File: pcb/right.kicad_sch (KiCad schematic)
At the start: 73 parts, among them J2 AudioJack3, SW22 Y, SW23 U, SW24 I, SW25 O, SW26 P, SW27 BS, SW28 H, SW29 J, SW30 K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

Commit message: Rewire left half
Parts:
- SW49: value T -> EX3
- SW50: value G -> EX4
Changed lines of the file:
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@@
 			)
 		)
-		(property "Value" "T"
+		(property "Value" "EX3"
 			(at 171.45 58.42 0)
 			(effects
@@
 			)
 		)
-		(property "Value" "G"
+		(property "Value" "EX4"
 			(at 171.45 83.82 0)
 			(effects

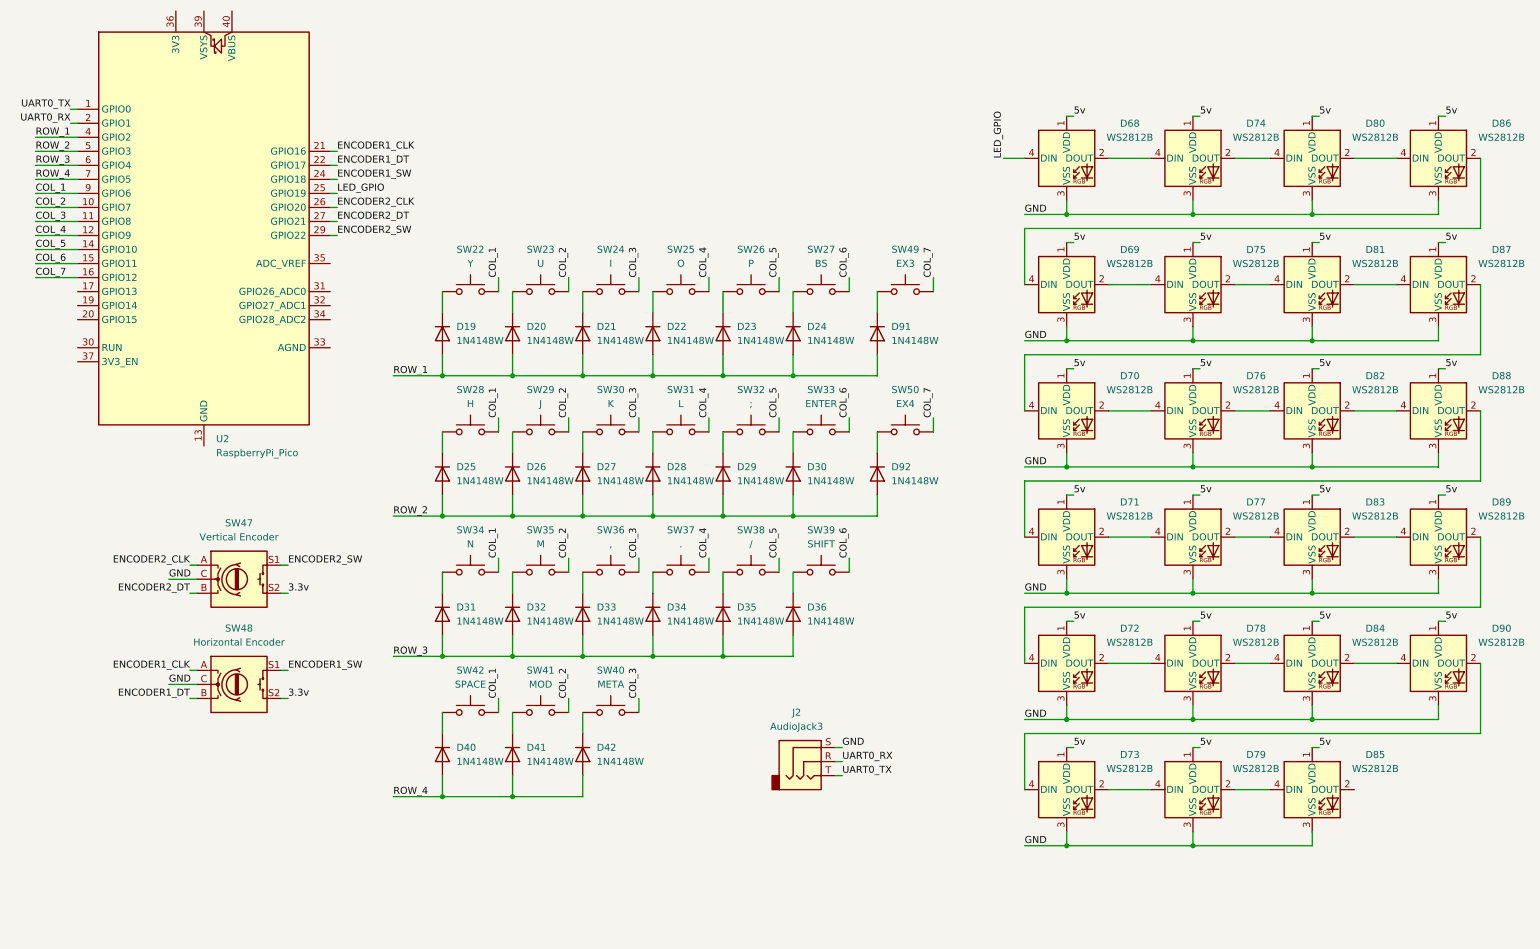
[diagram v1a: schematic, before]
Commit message: Move row and column to start with 0 on schematic
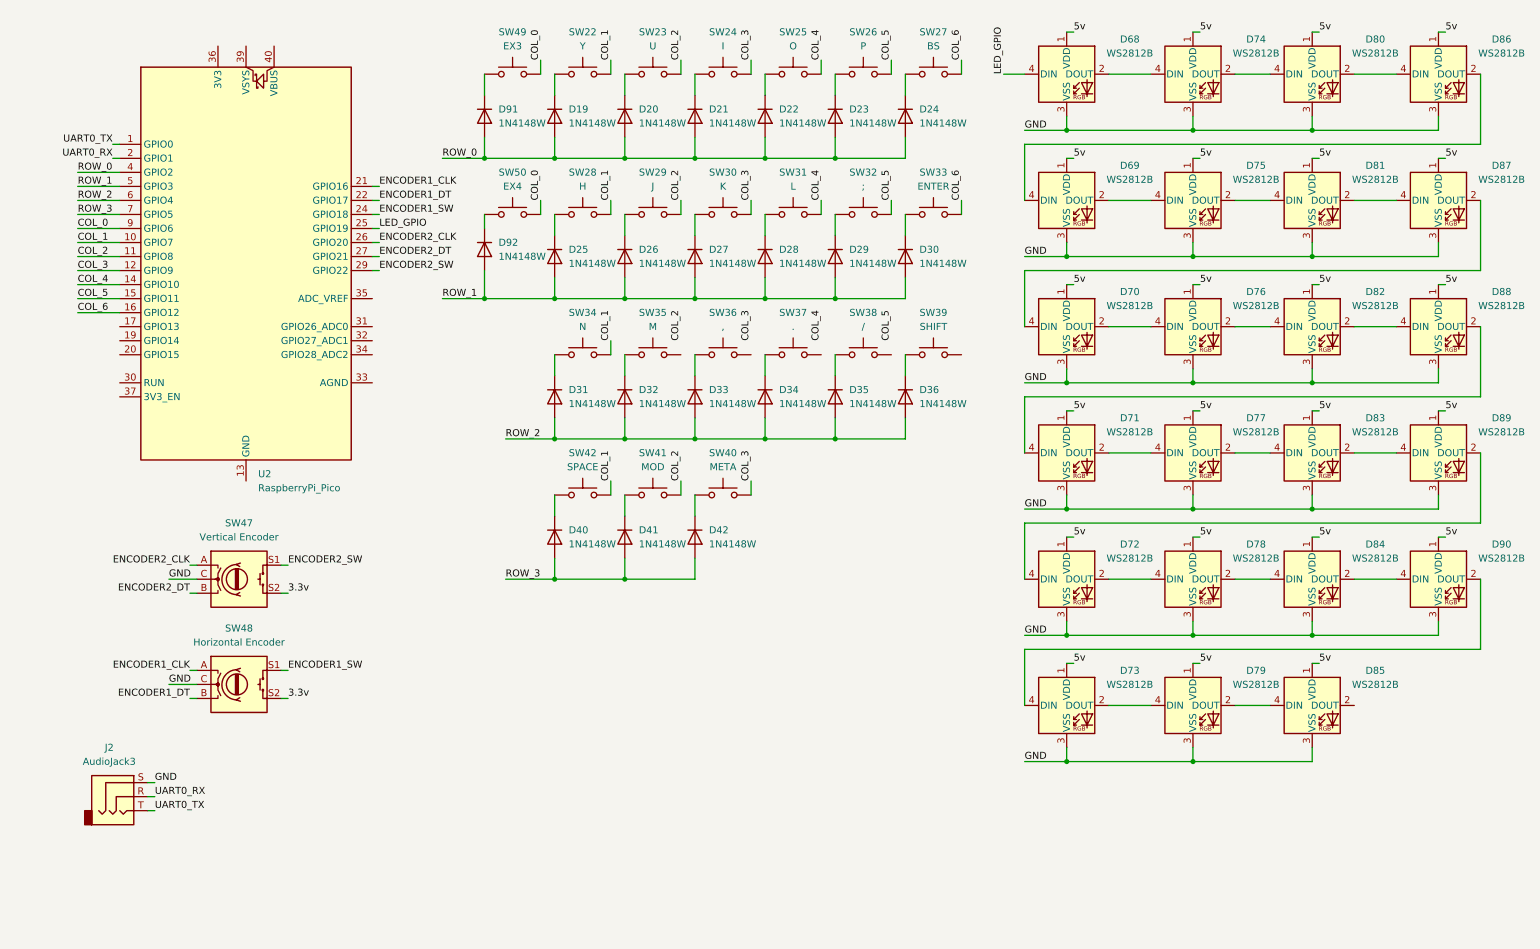
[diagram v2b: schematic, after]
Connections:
- net ROW_4 is gone; now on net ROW_3: D40.2 (A), D41.2 (A), D42.2 (A), U2.7 (GPIO5)
- net COL_1: now also U2.10 (GPIO7); no longer U2.9 (GPIO6)
- net COL_2: now also U2.11 (GPIO8); no longer SW35.2, U2.10 (GPIO7)
- net COL_3: now also U2.12 (GPIO9); no longer SW36.2, U2.11 (GPIO8)
- net COL_4: now also U2.14 (GPIO10); no longer SW37.2, U2.12 (GPIO9)
- net COL_5: now also U2.15 (GPIO11); no longer SW38.2, U2.14 (GPIO10)
- net COL_6: now also U2.16 (GPIO12); no longer SW39.2, U2.15 (GPIO11)
- net ROW_1: now also D25.2 (A), D26.2 (A), D27.2 (A), D28.2 (A), D29.2 (A), D30.2 (A), D92.2 (A), U2.5 (GPIO3); no longer D19.2 (A), D20.2 (A), D21.2 (A), D22.2 (A), D23.2 (A), D24.2 (A), D91.2 (A), U2.4 (GPIO2)
- net ROW_2: now also D31.2 (A), D32.2 (A), D33.2 (A), D34.2 (A), D35.2 (A), D36.2 (A), U2.6 (GPIO4); no longer D25.2 (A), D26.2 (A), D27.2 (A), D28.2 (A), D29.2 (A), D30.2 (A), D92.2 (A), U2.5 (GPIO3)
- net ROW_3: no longer D31.2 (A), D32.2 (A), D33.2 (A), D34.2 (A), D35.2 (A), D36.2 (A), U2.6 (GPIO4)
- net COL_7 renamed COL_0
- net COL_0: now also U2.9 (GPIO6); no longer U2.16 (GPIO12)
- new net ROW_0: D19.2 (A), D20.2 (A), D21.2 (A), D22.2 (A), D23.2 (A), D24.2 (A), D91.2 (A), U2.4 (GPIO2)
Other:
- moved on the sheet: D19, D20, D21, D22, D23, D24, D25, D26, D27, D28, D29, D30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

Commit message: Switch to RP2040 chip on board
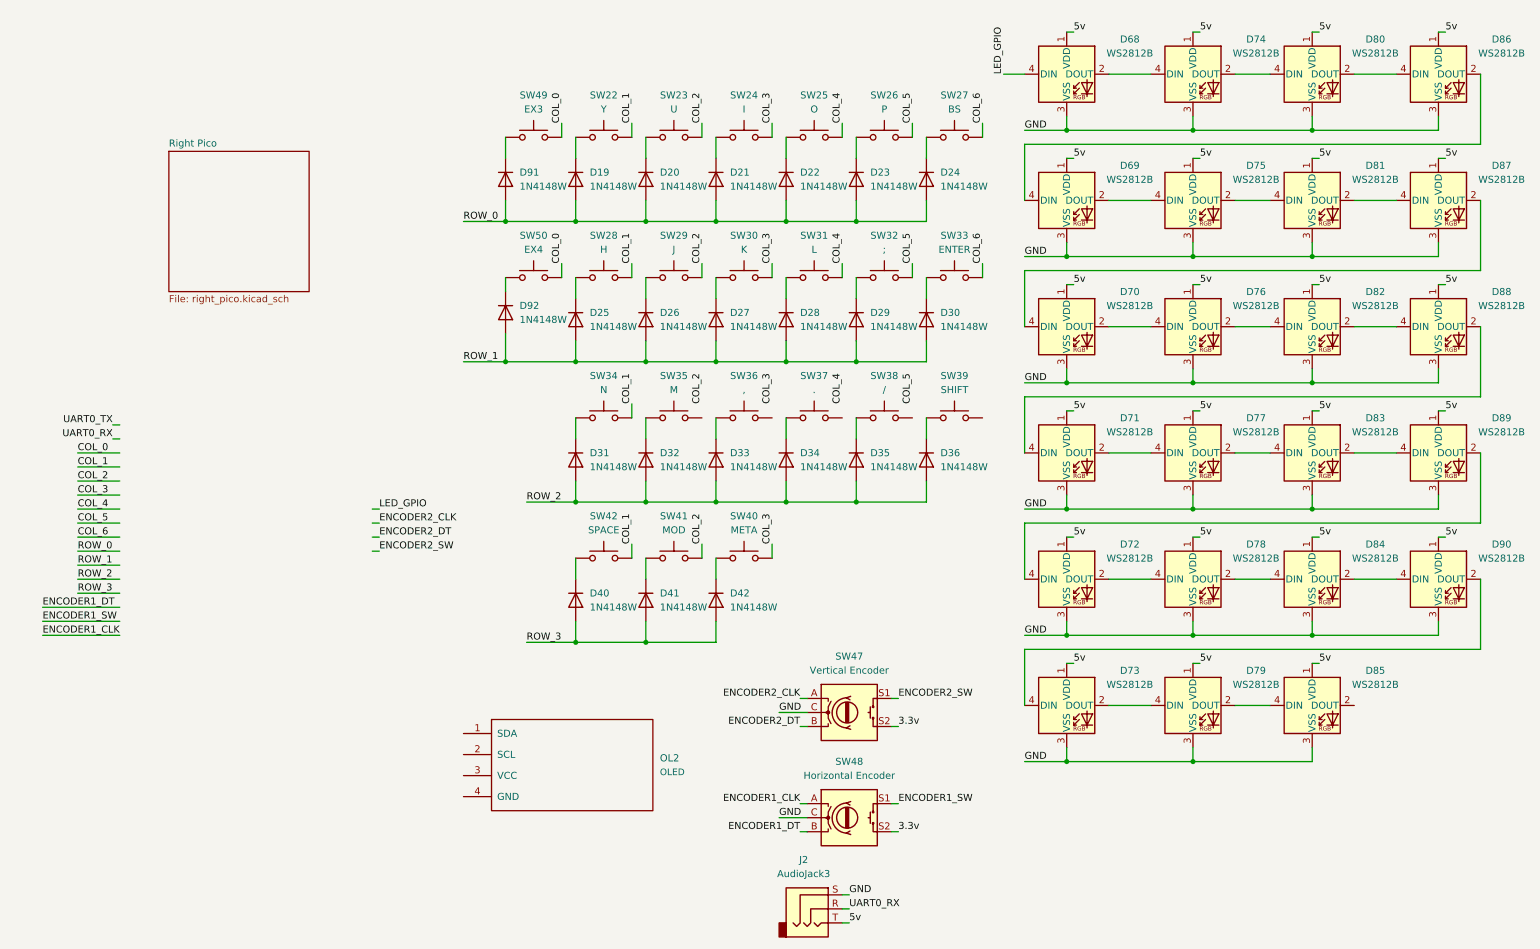
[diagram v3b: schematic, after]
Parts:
- removed U2: RaspberryPi_Pico, Module_RaspberryPi_Pico:RaspberryPi_Pico_Common, symbol MCU_Module_RaspberryPi_Pico:RaspberryPi_Pico
- added OL2: OLED, oled:SSD1306-0.91-OLED-4pin-128x32, symbol kbd:OLED
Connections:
- net 5v: now also J2.T
- net UART0_TX: no longer J2.T
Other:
- added sheet Right Pico (right_pico.kicad_sch)
- moved on the sheet: D19, D20, D21, D22, D23, D24, D25, D26, D27, D28, D29, D30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
